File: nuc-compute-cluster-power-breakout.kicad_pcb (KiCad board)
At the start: 4 copper layers, 100 x 100 mm, 126 parts, among them J1 USB3106-30-0230-A, J2 CONN_BM04B-SRSS-TB_LF__SN_, J3 CONN_BM04B-SRSS-TB_LF__SN_, J4 Conn_01x10, J5 430450812, J6 430450812, J7 430450812, J8 430450812, J9 430450812, Q1 SQS401EN-T1_BE3, Q10 SOT-883, Q15 DMN4010LFG-7, Q2 SQS401EN-T1_BE3, Q3 SOT-883, Q4 SOT-883, Q5 SQS401EN-T1_BE3, Q6 SOT-883, Q7 SQS401EN-T1_BE3, Q8 SQS401EN-T1_BE3, Q9 SOT-883, U1 FT2232HL-REEL, U10 TCA9534, U11 TMCS1100A2-Q1, U12 TMCS1100A2-Q1, U13 TMCS1100A2-Q1, U14 ADS7828, U15 AP62301WU-7, U7 AP62301WU-7, U8 TMCS1100A2-Q1, U9 TMCS1100A2-Q1, Y1 KX-7_12,MHz

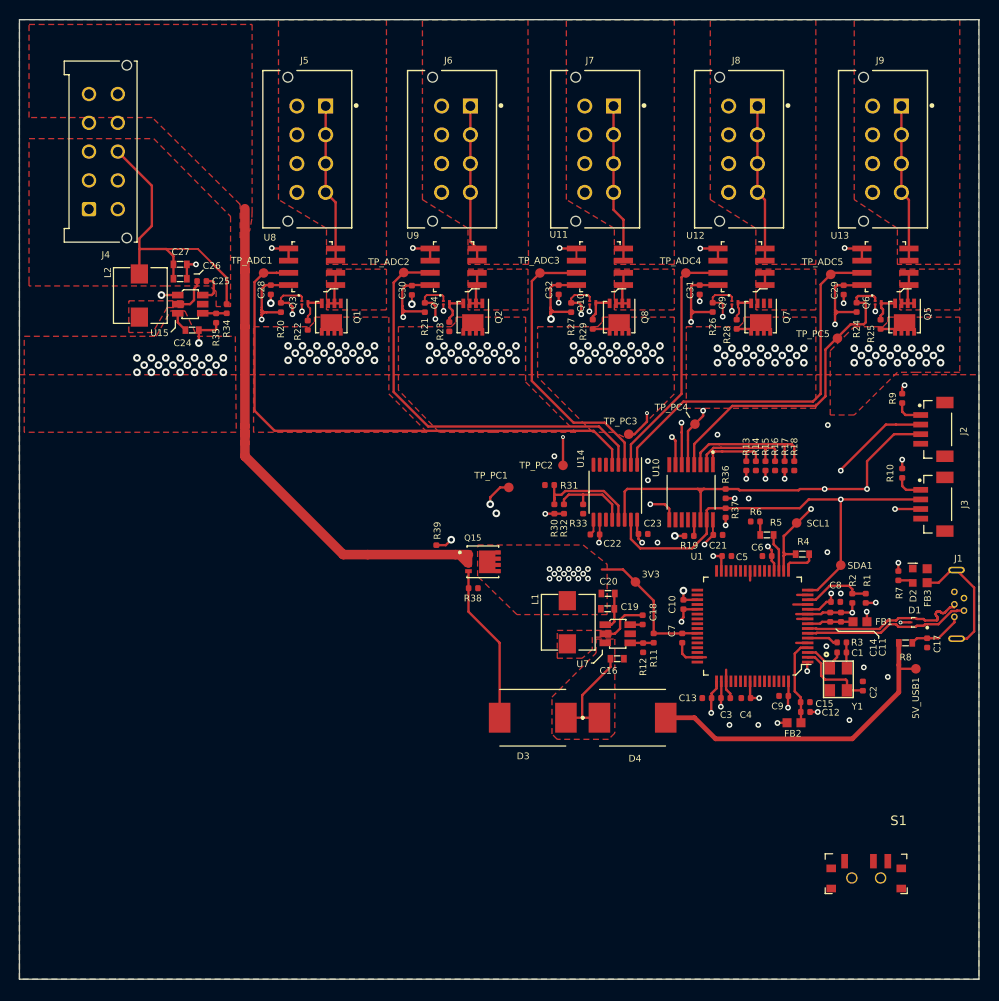
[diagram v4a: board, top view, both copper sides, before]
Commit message: Added power switch. PCB update.
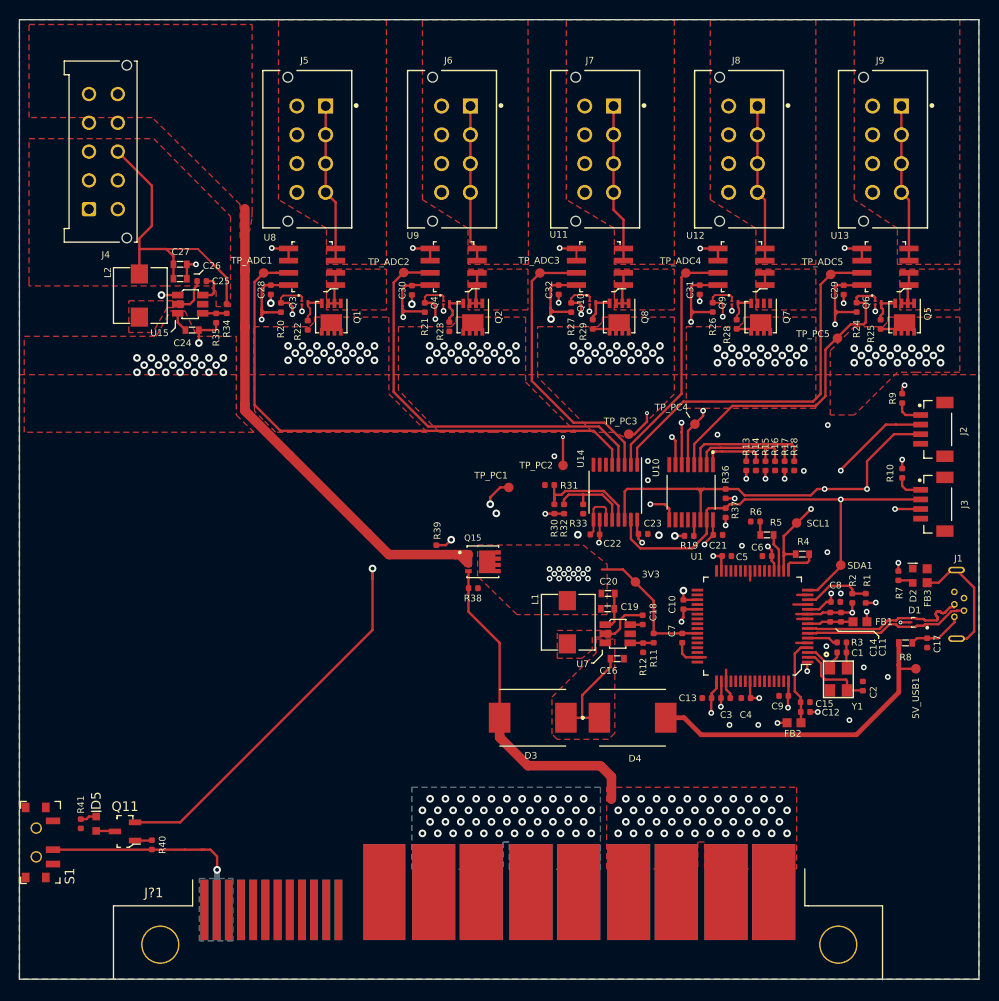
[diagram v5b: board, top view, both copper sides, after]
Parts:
- added D5: LG_L29K-G2J1-24-Z, antmicro-footprints:LED_0603, F.Cu at (98.0, 133.8)
- added J?1: 10107844-002LF, antmicro-footprints:10107844-002LF, F.Cu at (139.4, 150.0)
- added Q11: BC856,215, antmicro-footprints:SOT-23-3, F.Cu at (101.0, 134.6)
- added R40: R_10k_0402, antmicro-footprints:0402-res, F.Cu at (103.8, 136.0)
- added R41: R_680R_0402, antmicro-footprints:0402-res, F.Cu at (96.4, 133.8)
- J2, J3: value CONN_BM04B-SRSS-TB_LF__SN_ -> BM04B-SRSS-TB-LF-SN
- J4: value Conn_01x10 -> 43045-1013
- Q10, Q3, Q4, Q6, Q9: value SOT-883 -> SSM3K15ACT
- moved S1 86.6 mm to (91.8, 135.8), turned to 270 degrees
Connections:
- J3 pad 4: GND -> Net-(J3-Pad4)
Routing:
- net VCC3V3: track 206.4 -> 253.9 mm, vias 43 -> 44
- net VCC12V0: track 27.9 -> 63.2 mm, vias 120 -> 166
- net PSU_ON: track 0.00 -> 23.0 mm, vias 0 -> 1
- net GND: track 67.3 -> 87.8 mm, vias 36 -> 84
- net DB_3V3: track 59.0 -> 54.9 mm
- net Net-(D5-Pad1): track 0.00 -> 1.97 mm
- net Net-(Q11-Pad1): track 0.00 -> 1.76 mm
- net Net-(D5-Pad2): track 0.00 -> 1.71 mm
- added copper zone on B.Cu, net GND
- added copper zone on B.Cu, net PSU_ON

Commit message: Added stitching and mounting holes
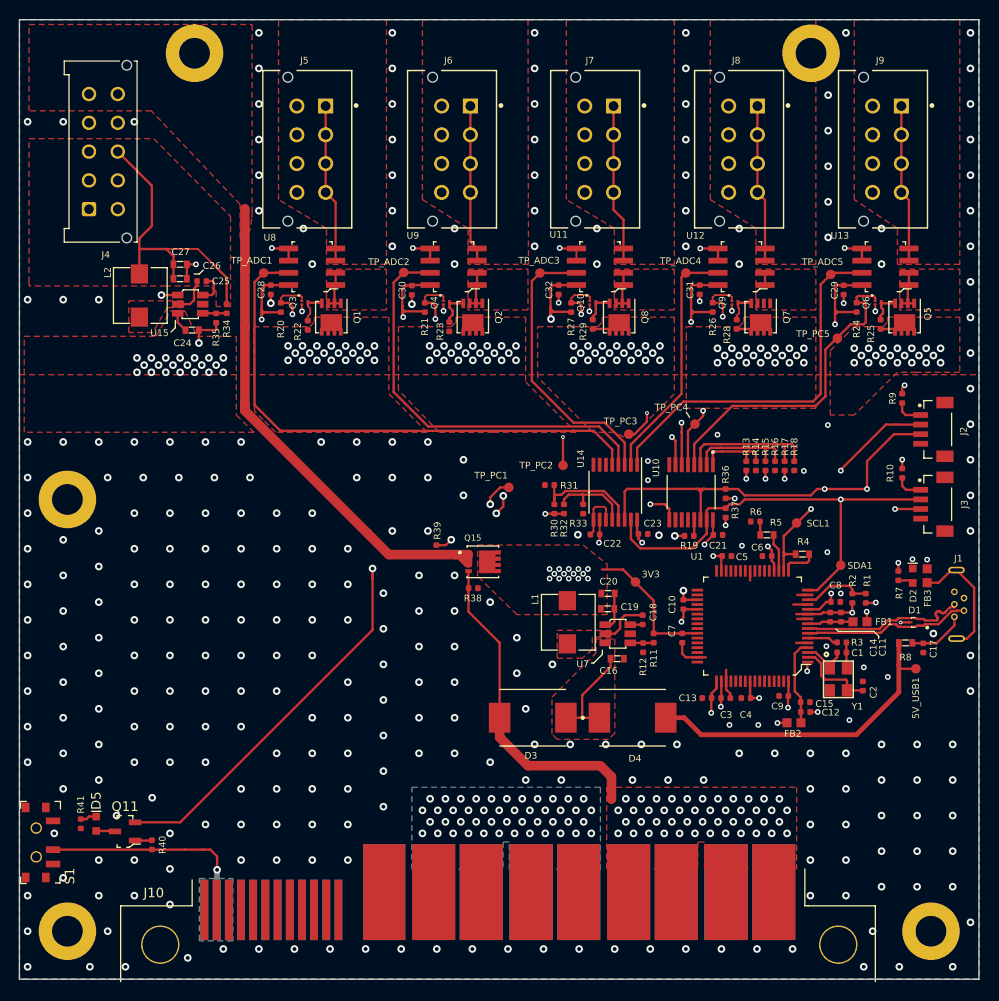
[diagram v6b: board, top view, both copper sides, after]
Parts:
- added MP1: PCB_Mount_Hole_3mm_6mm_pad, antmicro-footprints:mounting-hole-3.2mm, F.Cu at (95.0, 100.0)
- added MP2: PCB_Mount_Hole_3mm_6mm_pad, antmicro-footprints:mounting-hole-3.2mm, F.Cu at (95.0, 145.0)
- added MP3: PCB_Mount_Hole_3mm_6mm_pad, antmicro-footprints:mounting-hole-3.2mm, F.Cu at (172.5, 53.5)
- added MP4: PCB_Mount_Hole_3mm_6mm_pad, antmicro-footprints:mounting-hole-3.2mm, F.Cu at (185.0, 145.0)
- added MP5: PCB_Mount_Hole_3mm_6mm_pad, antmicro-footprints:mounting-hole-3.2mm, F.Cu at (108.2, 53.5)
- moved C17 0.66 mm to (184.2, 115.5)
- renumbered J?1 to J10
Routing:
- net VCC3V3: track 253.9 -> 247.3 mm
- net GND: vias 84 -> 367
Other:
- board text removed: "TODO: Add footprint of the edge connector"
- board text removed: "TODO: Add some mounting holes"
- board text removed: "TODO: Update missing 3D models (minor issue)"

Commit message: Loclib performed
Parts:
- D5: footprint antmicro-footprints:LED_0603 -> nuc-compute-cluster-power-breakout-footprints:LED_0603
- J10: footprint antmicro-footprints:10107844-002LF -> nuc-compute-cluster-power-breakout-footprints:10107844-002LF
- MP1, MP2, MP3, MP4, MP5: footprint antmicro-footprints:mounting-hole-3.2mm -> nuc-compute-cluster-power-breakout-footprints:mounting-hole-3.2mm
- Q11: footprint antmicro-footprints:SOT-23-3 -> nuc-compute-cluster-power-breakout-footprints:SOT-23-3
- Q15: footprint antmicro-footprints:POWERVDFN-8 -> nuc-compute-cluster-power-breakout-footprints:POWERVDFN-8
- R38, R39, R40, R41: footprint antmicro-footprints:0402-res -> nuc-compute-cluster-power-breakout-footprints:0402-res
- S1: footprint antmicro-footprints:Switch_Slide_MSS3 -> nuc-compute-cluster-power-breakout-footprints:Switch_Slide_MSS3
- TP_ADC1, TP_ADC2, TP_ADC3, TP_ADC4, TP_ADC5, TP_PC1, TP_PC2, TP_PC3, TP_PC4, TP_PC5: footprint antmicro-footprints:Testpoint_smd_1mm -> nuc-compute-cluster-power-breakout-footprints:Testpoint_smd_1mm
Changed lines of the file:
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@@
     (add_net /FTDI/USB_D-)
   )
-  (module antmicro-footprints:POWERVDFN-8 (layer F.Cu)
+  (module nuc-compute-cluster-power-breakout-footprints:POWERVDFN-8 (layer F.Cu)
     (at 138.3 106.5)
     (fp_text reference Q15 (at -1.05 -2.5) (layer F.SilkS)
@@
       (net 14 VCC12V0))
   )
-  (module antmicro-footprints:mounting-hole-3.2mm (layer F.Cu)
+  (module nuc-compute-cluster-power-breakout-footprints:mounting-hole-3.2mm (layer F.Cu)
     (at 108.25 53.5)
     (fp_text reference MP5 (at -0.1778 4.0259) (layer F.SilkS) hide
@@
       (net 4 GND))
   )
-  (module antmicro-footprints:mounting-hole-3.2mm (layer F.Cu)
+  (module nuc-compute-cluster-power-breakout-footprints:mounting-hole-3.2mm (layer F.Cu)
     (at 185 145)
     (fp_text reference MP4 (at -0.1778 4.0259) (layer F.SilkS) hide
@@
       (net 4 GND))
   )
-  (module antmicro-footprints:mounting-hole-3.2mm (layer F.Cu)
+  (module nuc-compute-cluster-power-breakout-footprints:mounting-hole-3.2mm (layer F.Cu)
     (at 172.5 53.5)
     (fp_text reference MP3 (at -0.1778 4.0259) (layer F.SilkS) hide
@@
       (net 4 GND))
   )
-  (module antmicro-footprints:mounting-hole-3.2mm (layer F.Cu)
+  (module nuc-compute-cluster-power-breakout-footprints:mounting-hole-3.2mm (layer F.Cu)
     (at 95 145)
     (fp_text reference MP2 (at -0.1778 4.0259) (layer F.SilkS) hide
@@
       (net 4 GND))
   )
-  (module antmicro-footprints:mounting-hole-3.2mm (layer F.Cu)
+  (module nuc-compute-cluster-power-breakout-footprints:mounting-hole-3.2mm (layer F.Cu)
     (at 95 100)
     (fp_text reference MP1 (at -0.1778 4.0259) (layer F.SilkS) hide
@@
       (net 4 GND))
   )
-  (module antmicro-footprints:10107844-002LF (layer F.Cu)
+  (module nuc-compute-cluster-power-breakout-footprints:10107844-002LF (layer F.Cu)
     (at 139.45 150)
     (fp_text reference J10 (at -35.45 -9) (layer F.SilkS)
@@
     (pad P29/30 smd rect (at 14.0375 -9.08 90) (size 10 4.495) (layers B.Cu)
       (net 14 VCC12V0))
-    (model ${ANT3DMDL}/10107844-002lf.stp
+    (model ${KIPRJMOD}/lib/3d-models/10107844-002lf.stp
       (offset (xyz 0 3.6 3.75))
       (scale (xyz 1 1 1))
@@
     )
   )
-  (module antmicro-footprints:0402-res (layer F.Cu)
+  (module nuc-compute-cluster-power-breakout-footprints:0402-res (layer F.Cu)
     (at 96.4 133.8 270)
     (descr "Resistor SMD 0402 (1005 Metric), square (rectangular) end terminal, IPC_7351 nominal, (Body size source: http://www.tortai-tech.com/upload/download/2011102023233369053.pdf), generated with kicad-footprint-generator")
@@
     (pad 1 smd roundrect (at -0.485 0 270) (size 0.59 0.64) (layers F.Cu F.Paste F.Mask) (roundrect_rratio 0.25)
       (net 110 "Net-(D5-Pad2)"))
-    (model ${ANT3DMDL}/0402-res.step
+    (model ${KIPRJMOD}/lib/3d-models/0402-res.step
       (offset (xyz 0 0 -0.01))
       (scale (xyz 1 1 1))
@@
     )
   )
-  (module antmicro-footprints:0402-res (layer F.Cu)
+  (module nuc-compute-cluster-power-breakout-footprints:0402-res (layer F.Cu)
     (at 103.8 136 270)
     (descr "Resistor SMD 0402 (1005 Metric), square (rectangular) end terminal, IPC_7351 nominal, (Body size source: http://www.tortai-tech.com/upload/download/2011102023233369053.pdf), generated with kicad-footprint-generator")
@@
     (pad 1 smd roundrect (at -0.485 0 270) (size 0.59 0.64) (layers F.Cu F.Paste F.Mask) (roundrect_rratio 0.25)
       (net 111 "Net-(Q11-Pad1)"))
-    (model ${ANT3DMDL}/0402-res.step
+    (model ${KIPRJMOD}/lib/3d-models/0402-res.step
       (offset (xyz 0 0 -0.01))
       (scale (xyz 1 1 1))
@@
     )
   )
-  (module antmicro-footprints:SOT-23-3 (layer F.Cu)
+  (module nuc-compute-cluster-power-breakout-footprints:SOT-23-3 (layer F.Cu)
     (at 101 134.6 180)
     (attr smd)
@@
     (pad 3 smd rect (at 1.05 0 180) (size 1.3 0.6) (layers F.Cu F.Paste F.Mask)
       (net 109 "Net-(D5-Pad1)") (solder_mask_margin 0.07))
-    (model ${ANT3DMDL}/sot23-3.step
+    (model ${KIPRJMOD}/lib/3d-models/sot23-3.step
       (offset (xyz 0 0 0.35))
       (scale (xyz 1 1 1))
@@
     )
   )
-  (module antmicro-footprints:LED_0603 (layer F.Cu)
+  (module nuc-compute-cluster-power-breakout-footprints:LED_0603 (layer F.Cu)
     (at 98 133.8 270)
     (attr smd)
@@
     (pad 2 smd rect (at -0.75 0 270) (size 0.8 0.8) (layers F.Cu F.Paste F.Mask)
       (net 110 "Net-(D5-Pad2)"))
-    (model ${ANT3DMDL}/LED0603.step
+    (model ${KIPRJMOD}/lib/3d-models/LED0603.step
       (at (xyz 0 0 0))
       (scale (xyz 1 1 1))
@@
     )
   )
-  (module antmicro-footprints:Testpoint_smd_1mm (layer F.Cu)
+  (module nuc-compute-cluster-power-breakout-footprints:Testpoint_smd_1mm (layer F.Cu)
     (at 175.25 83.25)
     (attr virtual)
@@
       (net 33 "/Power Cycling & Current Measurement/PC_5"))
   )
-  (module antmicro-footprints:Testpoint_smd_1mm (layer F.Cu)
+  (module nuc-compute-cluster-power-breakout-footprints:Testpoint_smd_1mm (layer F.Cu)
     (at 160.4 92.2)
     (attr virtual)
@@
       (net 38 "/Power Cycling & Current Measurement/PC_4"))
   )
-  (module antmicro-footprints:Testpoint_smd_1mm (layer F.Cu)
+  (module nuc-compute-cluster-power-breakout-footprints:Testpoint_smd_1mm (layer F.Cu)
     (at 153.5 93.2508)
     (attr virtual)
@@
       (net 39 "/Power Cycling & Current Measurement/PC_3"))
   )
-  (module antmicro-footprints:Testpoint_smd_1mm (layer F.Cu)
+  (module nuc-compute-cluster-power-breakout-footprints:Testpoint_smd_1mm (layer F.Cu)
     (at 146.65 96.5)
     (attr virtual)
@@
       (net 30 "/Power Cycling & Current Measurement/PC_2"))
   )
-  (module antmicro-footprints:Testpoint_smd_1mm (layer F.Cu)
+  (module nuc-compute-cluster-power-breakout-footprints:Testpoint_smd_1mm (layer F.Cu)
     (at 141 98.8)
     (attr virtual)
@@
       (net 29 "/Power Cycling & Current Measurement/PC_1"))
   )
-  (module antmicro-footprints:Testpoint_smd_1mm (layer F.Cu)
+  (module nuc-compute-cluster-power-breakout-footprints:Testpoint_smd_1mm (layer F.Cu)
     (at 174.55 76.6)
     (attr virtual)
@@
       (net 62 "/Power Cycling & Current Measurement/C_ADC5"))
   )
-  (module antmicro-footprints:Testpoint_smd_1mm (layer F.Cu)
+  (module nuc-compute-cluster-power-breakout-footprints:Testpoint_smd_1mm (layer F.Cu)
     (at 159.45 76.4508)
     (attr virtual)
@@
       (net 61 "/Power Cycling & Current Measurement/C_ADC4"))
   )
-  (module antmicro-footprints:Testpoint_smd_1mm (layer F.Cu)
+  (module nuc-compute-cluster-power-breakout-footprints:Testpoint_smd_1mm (layer F.Cu)
     (at 144.25 76.45)
     (attr virtual)
@@
       (net 60 "/Power Cycling & Current Measurement/C_ADC3"))
   )
-  (module antmicro-footprints:Testpoint_smd_1mm (layer F.Cu)
+  (module nuc-compute-cluster-power-breakout-footprints:Testpoint_smd_1mm (layer F.Cu)
     (at 130.05 76.4)
     (attr virtual)
@@
       (net 59 "/Power Cycling & Current Measurement/C_ADC2"))
   )
-  (module antmicro-footprints:Testpoint_smd_1mm (layer F.Cu)
+  (module nuc-compute-cluster-power-breakout-footprints:Testpoint_smd_1mm (layer F.Cu)
     (at 115.45 76.45)
     (attr virtual)
@@
       (net 58 "/Power Cycling & Current Measurement/C_ADC1"))
   )
-  (module antmicro-footprints:Switch_Slide_MSS3 (layer F.Cu)
+  (module nuc-compute-cluster-power-breakout-footprints:Switch_Slide_MSS3 (layer F.Cu)
     (at 91.75 135.75 270)
     (attr smd)
@@
     (pad 0 smd rect (at 3.65 -1 270) (size 1 0.8) (layers F.Cu F.Paste F.Mask))
     (pad 0 smd rect (at 3.65 1.1 270) (size 1 0.8) (layers F.Cu F.Paste F.Mask))
-    (model ${ANT3DMDL}/MSS3_slide_switch.step
+    (model ${KIPRJMOD}/lib/3d-models/MSS3_slide_switch.step
       (offset (xyz 0.55 -0.1 0))
       (scale (xyz 1 1 1))
@@
     )
   )
-  (module antmicro-footprints:0402-res (layer F.Cu)
+  (module nuc-compute-cluster-power-breakout-footprints:0402-res (layer F.Cu)
     (at 133.45 105.25 90)
     (descr "Resistor SMD 0402 (1005 Metric), square (rectangular) end terminal, IPC_7351 nominal, (Body size source: http://www.tortai-tech.com/upload/download/2011102023233369053.pdf), generated with kicad-footprint-generator")
@@
     (pad 1 smd roundrect (at -0.485 0 90) (size 0.59 0.64) (layers F.Cu F.Paste F.Mask) (roundrect_rratio 0.25)
       (net 64 DB_3V3))
-    (model ${ANT3DMDL}/0402-res.step
+    (model ${KIPRJMOD}/lib/3d-models/0402-res.step
       (offset (xyz 0 0 -0.01))
       (scale (xyz 1 1 1))
@@
     )
   )
-  (module antmicro-footprints:0402-res (layer F.Cu)
+  (module nuc-compute-cluster-power-breakout-footprints:0402-res (layer F.Cu)
     (at 137.3 109.25)
     (descr "Resistor SMD 0402 (1005 Metric), square (rectangular) end terminal, IPC_7351 nominal, (Body size source: http://www.tortai-tech.com/upload/download/2011102023233369053.pdf), generated with kicad-footprint-generator")
@@
     (pad 1 smd roundrect (at -0.485 0) (size 0.59 0.64) (layers F.Cu F.Paste F.Mask) (roundrect_rratio 0.25)
       (net 14 VCC12V0))
-    (model ${ANT3DMDL}/0402-res.step
+    (model ${KIPRJMOD}/lib/3d-models/0402-res.step
       (offset (xyz 0 0 -0.01))
       (scale (xyz 1 1 1))
@@
       (rotate (xyz 0 0 0))
     )
-    (model ${ANT3DMDL}/FT2232HL-REEL.step
+    (model ${KIPRJMOD}/lib/3d-models/FT2232HL-REEL.step
       (at (xyz 0 0 0))
       (scale (xyz 1 1 1))
